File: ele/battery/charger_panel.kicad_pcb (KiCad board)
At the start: 2 copper layers, 86.7 x 87.2 mm, 16 parts, among them J12 B1_M, J13 B2_P, J28 B2_M, J7 OUT, J8 B1_P, U1 ChinaLiIonCharger, U2 ChinaLiIonCharger

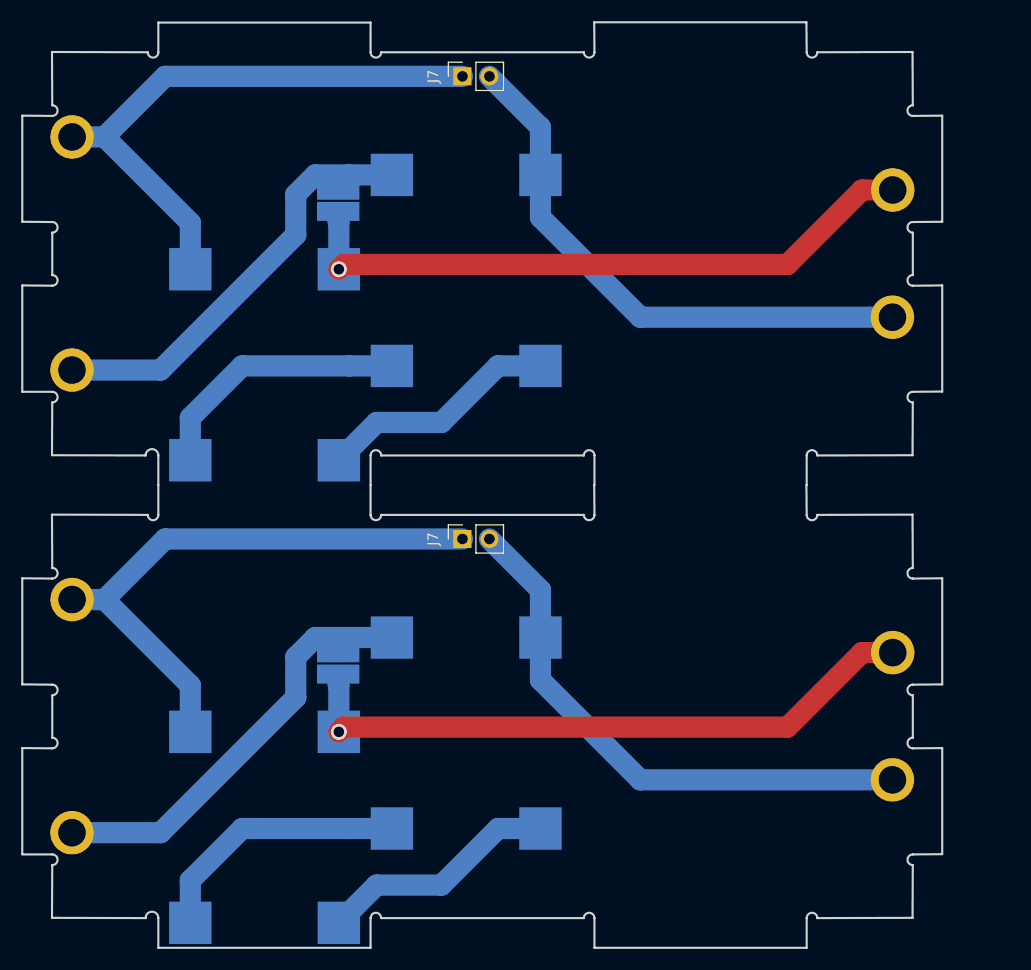
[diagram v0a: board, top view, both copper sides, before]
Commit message: ele: Update battery panels
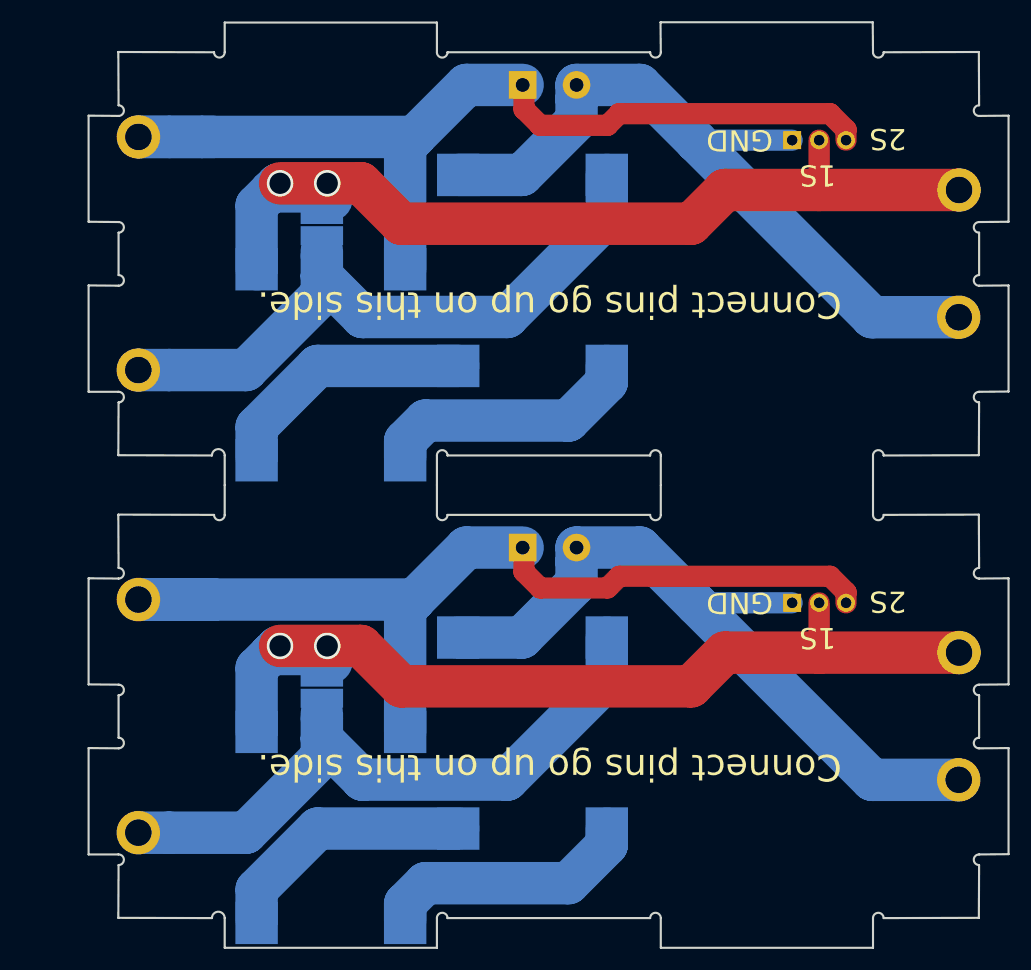
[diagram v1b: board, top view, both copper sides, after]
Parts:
- removed the J12 at (192.3, 90.4)
- removed the J12 at (192.3, 134.0)
- removed the J13 at (114.9, 107.3)
- removed the J13 at (114.9, 150.9)
- removed the J28 at (192.2, 102.4)
- removed the J28 at (192.2, 146.0)
- removed the J7 at (151.7, 79.7)
- removed the J7 at (151.7, 123.3)
- removed the J8 at (114.9, 85.4)
- removed the J8 at (114.9, 129.0)
- removed the JP1 at (140.0, 91.4)
- removed the JP1 at (140.0, 135.0)
- removed the U1 at (133.1, 106.8)
- removed the U1 at (133.1, 150.4)
- removed the U2 at (152.1, 98.0)
- removed the U2 at (152.1, 141.6)
- added J12: B1_M, yaqwsx:banana_2mm_hole, F.Cu at (198.5, 134.0)
- added J12: B1_M, yaqwsx:banana_2mm_hole, F.Cu at (198.5, 90.4)
- added J13: B2_P, yaqwsx:banana_2mm_hole, F.Cu at (121.2, 150.9)
- added J13: B2_P, yaqwsx:banana_2mm_hole, F.Cu at (121.2, 107.3)
- added J28: B2_M, yaqwsx:banana_2mm_hole, F.Cu at (198.5, 146.0)
- added J28: B2_M, yaqwsx:banana_2mm_hole, F.Cu at (198.5, 102.4)
- added J29: Balancer, Connector_PinSocket_2.54mm:PinSocket_1x03_P2.54mm_Horizontal, B.Cu at (182.8, 129.3)
- added J29: Balancer, Connector_PinSocket_2.54mm:PinSocket_1x03_P2.54mm_Horizontal, B.Cu at (182.8, 85.7)
- added J7: OUT, BATTERY:2_pads_5mm, B.Cu at (157.4, 124.1)
- added J7: OUT, BATTERY:2_pads_5mm, B.Cu at (157.4, 80.5)
- added J8: B1_P, yaqwsx:banana_2mm_hole, F.Cu at (121.2, 129.0)
- added J8: B1_P, yaqwsx:banana_2mm_hole, F.Cu at (121.2, 85.4)
- added JP1: Jumper_NC_Small, yaqwsx:power_solder_jumper, B.Cu at (138.5, 137.3)
- added JP1: Jumper_NC_Small, yaqwsx:power_solder_jumper, B.Cu at (138.5, 93.7)
- added U1: ChinaLiIonCharger, yaqwsx:LiOnCharger, B.Cu at (139.3, 150.4)
- added U1: ChinaLiIonCharger, yaqwsx:LiOnCharger, B.Cu at (139.3, 106.8)
- added U2: ChinaLiIonCharger, yaqwsx:LiOnCharger, B.Cu at (158.3, 141.6)
- added U2: ChinaLiIonCharger, yaqwsx:LiOnCharger, B.Cu at (158.3, 98.0)
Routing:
- net /B1_P_ch: track 109.9 -> 187.2 mm
- net /B1_M_ch: track 120.7 -> 185.9 mm, vias 2 -> 4
- net /B2_P_ch: track 82.9 -> 132.3 mm
- net Net-(U1-Pad2): track 50.1 -> 98.6 mm
- net /B2_M_ch: track 104.7 -> 145.8 mm
- net Net-(U1-Pad1): track 45.4 -> 48.8 mm
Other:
- board text added: "+"
- board text added: "-"
- board text added: "1S"
- board text added: "2S"
- board text added: "<-"
- board text added: "Connect ->Dock Disconnect ->Charger"
- board text added: "Connect pins go up on this side."
- board text added: "GND"
- board text added: "Mickoflus Charger/Dock v0.3 04/2019 RobotikaBrno.cz"
- board text added: "github: roboticsbrno/ RB3201-RBControl"

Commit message: ele: Update battery panels
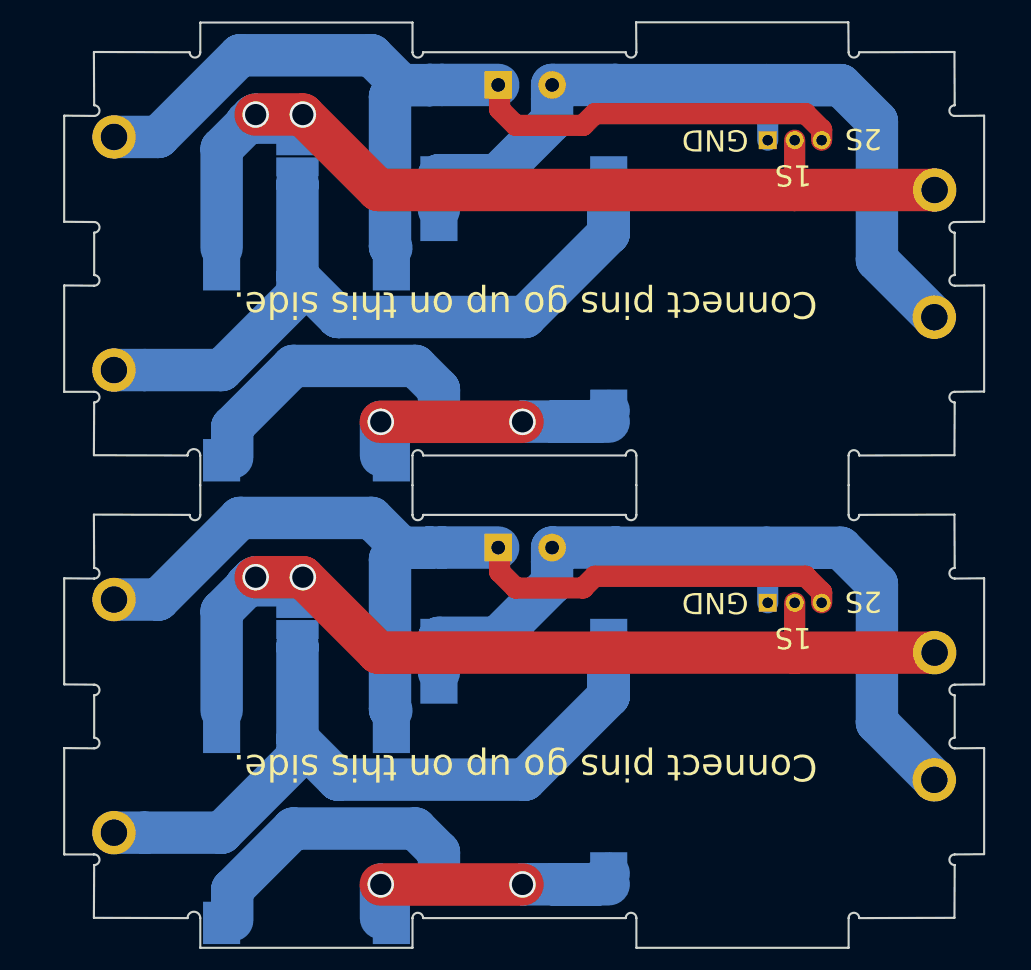
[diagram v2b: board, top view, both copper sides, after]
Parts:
- removed the J12 at (198.5, 134.0)
- removed the J12 at (198.5, 90.4)
- removed the J13 at (121.2, 150.9)
- removed the J13 at (121.2, 107.3)
- removed the J28 at (198.5, 146.0)
- removed the J28 at (198.5, 102.4)
- removed the J29 at (182.8, 129.3)
- removed the J29 at (182.8, 85.7)
- removed the J7 at (157.4, 124.1)
- removed the J7 at (157.4, 80.5)
- removed the J8 at (121.2, 129.0)
- removed the J8 at (121.2, 85.4)
- removed the JP1 at (138.5, 137.3)
- removed the JP1 at (138.5, 93.7)
- removed the U1 at (139.3, 150.4)
- removed the U1 at (139.3, 106.8)
- removed the U2 at (158.3, 141.6)
- removed the U2 at (158.3, 98.0)
- added J12: B1_M, yaqwsx:banana_2mm_hole, F.Cu at (196.2, 134.0)
- added J12: B1_M, yaqwsx:banana_2mm_hole, F.Cu at (196.2, 90.4)
- added J13: B2_P, yaqwsx:banana_2mm_hole, F.Cu at (118.9, 150.9)
- added J13: B2_P, yaqwsx:banana_2mm_hole, F.Cu at (118.9, 107.3)
- added J28: B2_M, yaqwsx:banana_2mm_hole, F.Cu at (196.2, 146.0)
- added J28: B2_M, yaqwsx:banana_2mm_hole, F.Cu at (196.2, 102.4)
- added J29: Balancer, Connector_PinSocket_2.54mm:PinSocket_1x03_P2.54mm_Horizontal, B.Cu at (180.5, 129.3)
- added J29: Balancer, Connector_PinSocket_2.54mm:PinSocket_1x03_P2.54mm_Horizontal, B.Cu at (180.5, 85.7)
- added J7: OUT, RB3201:2_pads_5mm, B.Cu at (155.1, 124.1)
- added J7: OUT, RB3201:2_pads_5mm, B.Cu at (155.1, 80.5)
- added J8: B1_P, yaqwsx:banana_2mm_hole, F.Cu at (118.9, 129.0)
- added J8: B1_P, yaqwsx:banana_2mm_hole, F.Cu at (118.9, 85.4)
- added JP1: Jumper_NC_Small, yaqwsx:power_solder_jumper, B.Cu at (136.2, 130.8)
- added JP1: Jumper_NC_Small, yaqwsx:power_solder_jumper, B.Cu at (136.2, 87.2)
- added U1: ChinaLiIonCharger, RB3201:LiOnCharger, B.Cu at (137.0, 150.4)
- added U1: ChinaLiIonCharger, RB3201:LiOnCharger, B.Cu at (137.0, 106.8)
- added U2: ChinaLiIonCharger, RB3201:LiOnCharger, B.Cu at (157.5, 145.8)
- added U2: ChinaLiIonCharger, RB3201:LiOnCharger, B.Cu at (157.5, 102.2)
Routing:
- net Net-(U1-Pad2): track 98.6 -> 77.2 mm
- net /B2_P_ch: track 132.3 -> 152.0 mm
- net /B2_M_ch: track 145.8 -> 158.9 mm
- net /B1_M_ch: track 185.9 -> 198.0 mm
- net Net-(U1-Pad1): track 48.8 -> 60.5 mm, vias 0 -> 4
- net /B1_P_ch: track 187.2 -> 183.6 mm
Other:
- board text added: "<----"
- board text added: "Mickoflus Charger/Dock v0.4 04/2019 RobotikaBrno.cz"
- board text removed: "<-"
- board text removed: "Mickoflus Charger/Dock v0.3 04/2019 RobotikaBrno.cz"
- board text removed: "github: roboticsbrno/ RB3201-RBControl"
